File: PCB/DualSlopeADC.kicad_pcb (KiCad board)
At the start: 2 copper layers, 43 x 69.9 mm, 25 parts, among them J2 Conn_01x02_Pin, J3 Conn_01x02_Pin, J5 Conn_01x02_Pin, J6 Conn_01x02_Pin, J7 Conn_01x02_Pin, J8 Conn_01x02_Pin, J9 Conn_01x02_Pin, U1 CH32V003FxPx, U2 ADR4533, U3 AD8605ARTZ-R2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

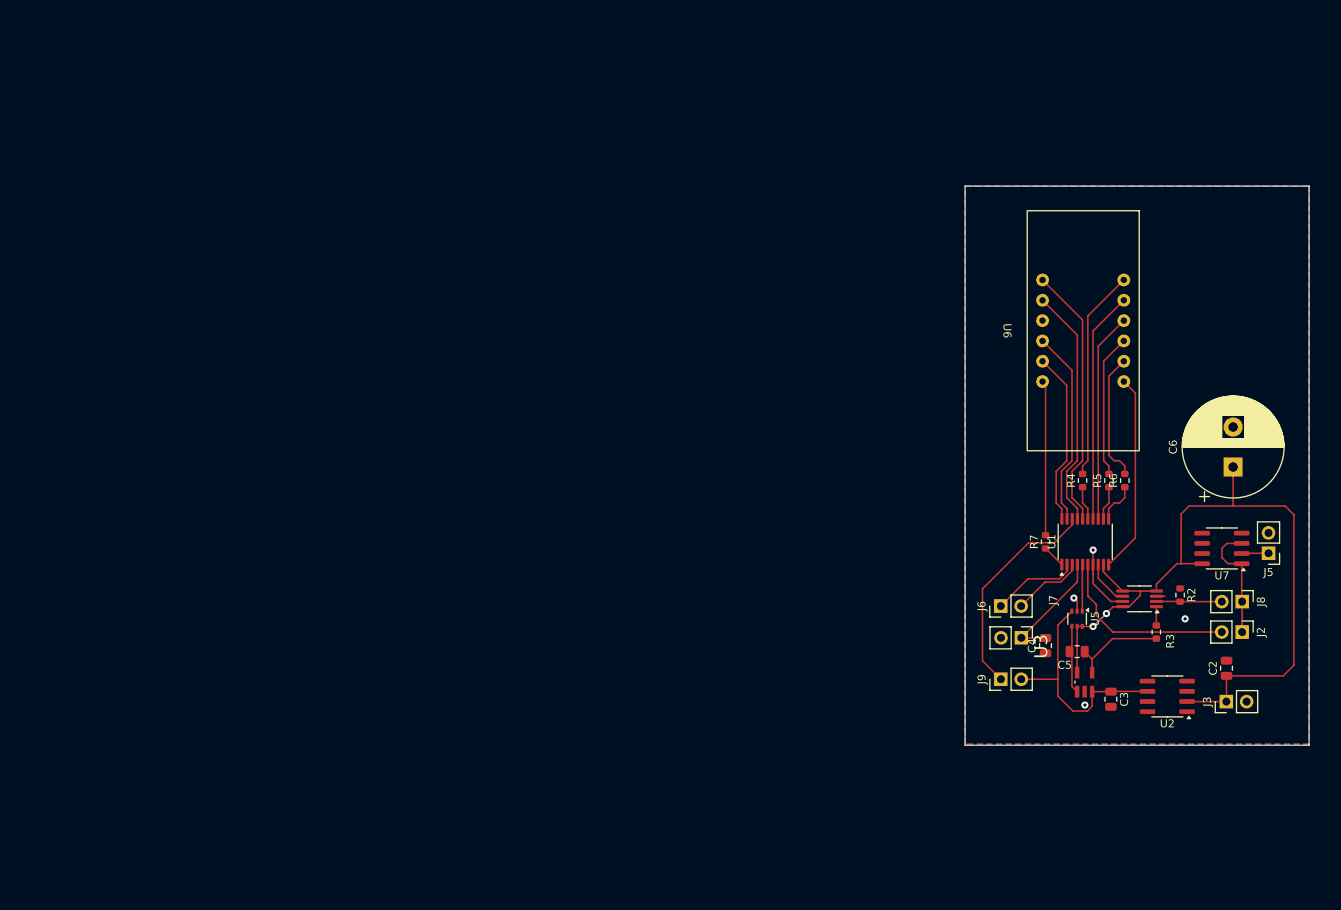
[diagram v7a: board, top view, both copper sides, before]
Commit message: Software ferrig, Timer einstellung auf basis das RC=100us, komplette gehirnschmelze wegen níchtlinearität durch offset sollte aber jetzt passen
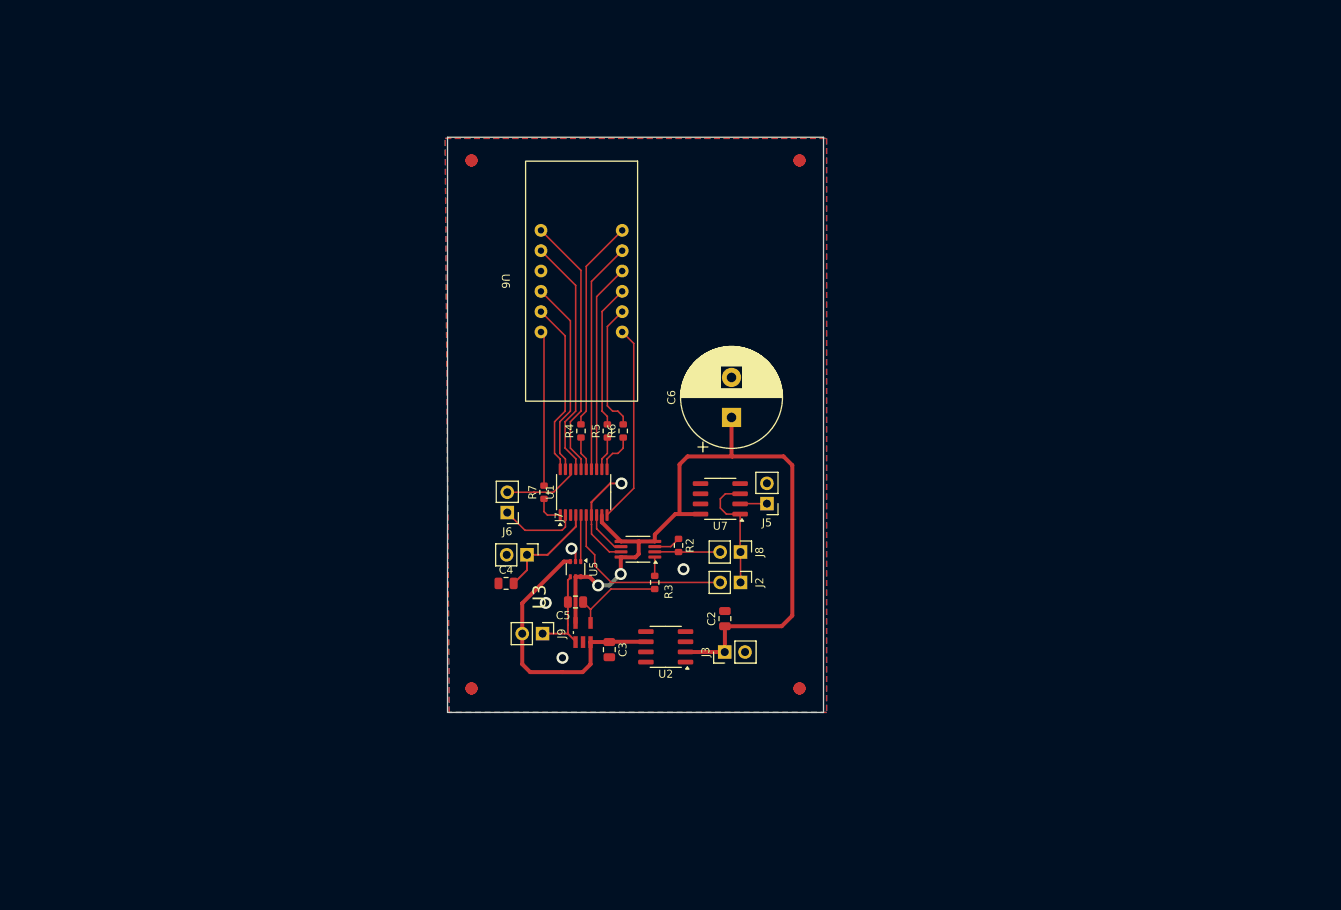
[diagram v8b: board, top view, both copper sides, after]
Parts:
- added ? (x3): , , F.Cu at (120.3, 126.8)
- added ? (x3): , , F.Cu at (120.3, 60.8)
- added ? (x3): , , F.Cu at (161.3, 126.8)
- added ? (x3): , , F.Cu at (161.3, 60.8)
- moved C4 67.9 mm to (124.6, 113.7), turned to 0 degrees
- moved C2 63.0 mm to (152.0, 118.1)
- moved J3 63.0 mm to (151.9, 122.2)
- moved J5 63.0 mm to (157.2, 103.7)
- moved R3 63.0 mm to (143.2, 113.5)
- moved R4 63.0 mm to (134.0, 94.6)
- moved R6 63.0 mm to (139.3, 94.6)
- moved U2 63.0 mm to (144.6, 121.6)
- moved U4 63.0 mm to (141.1, 109.4)
- moved C3 63.0 mm to (137.5, 122.0)
- moved C5 63.0 mm to (133.3, 116.0)
- moved C6 63.0 mm to (152.8, 92.9)
- moved J2 63.0 mm to (153.9, 113.5)
- moved J8 63.0 mm to (153.9, 109.8)
- moved R2 63.0 mm to (146.2, 108.9)
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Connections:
- C5 pad 2: Net-(U3-OUTA) -> out_int
- J6 pad 2: Rx -> SWIO
- J9 pad 1: SWIO -> out_int
- U1 pad 3: Rx -> unconnected-(U1-PD6-Pad3)
- U3 pad 1: Net-(U3-OUTA) -> out_int
- U5 pad 4: Net-(U3-OUTA) -> out_int
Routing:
- net SWIO: track 27.5 -> 9.54 mm
- net out_int: track 0.00 -> 11.6 mm
- net Rx: track 8.97 -> 0.00 mm
- net Net-(U3-OUTA): track 8.43 -> 0.00 mm
- net GND: track 11.7 -> 18.6 mm, vias 4 -> 5
- net VCC_3V3: track 30.0 -> 34.9 mm
- net VCC_5V: track 94.3 -> 96.9 mm
- net NRST: track 15.1 -> 13.3 mm
- net Tx: track 11.6 -> 9.85 mm
- net Net-(U1-PD4): track 2.87 -> 3.81 mm
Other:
- board size 43 x 69.9 mm -> 47 x 71.9 mm
